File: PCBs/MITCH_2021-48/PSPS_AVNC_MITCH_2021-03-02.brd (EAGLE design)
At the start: 25.4 x 58.1 mm, 58 parts, among them J1 A-1JB, J2 TFM-107-01-XXX-D-DS, U0-C STM32F411CEUX, U1-S ICM-20948, U11-S SN74LV1T34, U12-S SN74LV1T34, U13-S SN74LV1T34, U14-S SN74LV1T34, U14-S1 SN74LV1T34, U14-S2 SN74LV1T34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

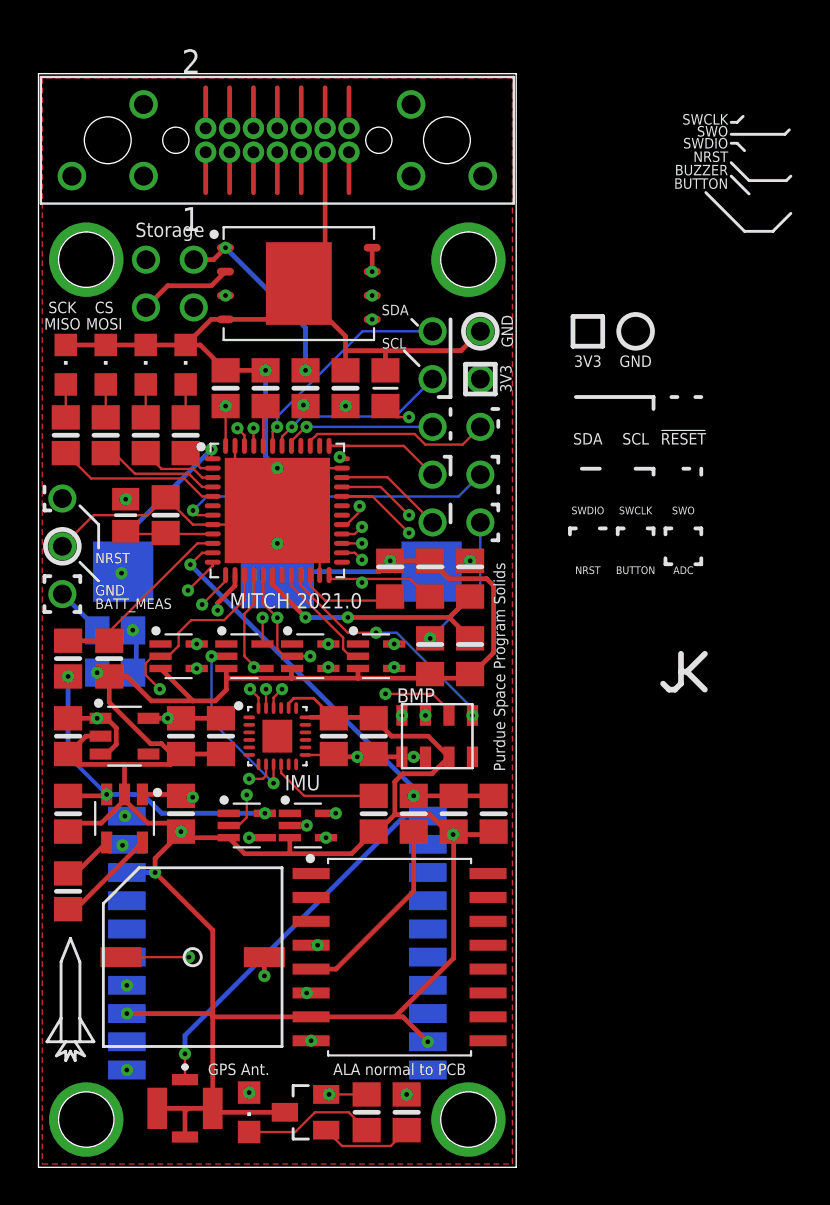
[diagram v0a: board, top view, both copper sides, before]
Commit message: Added separation notches
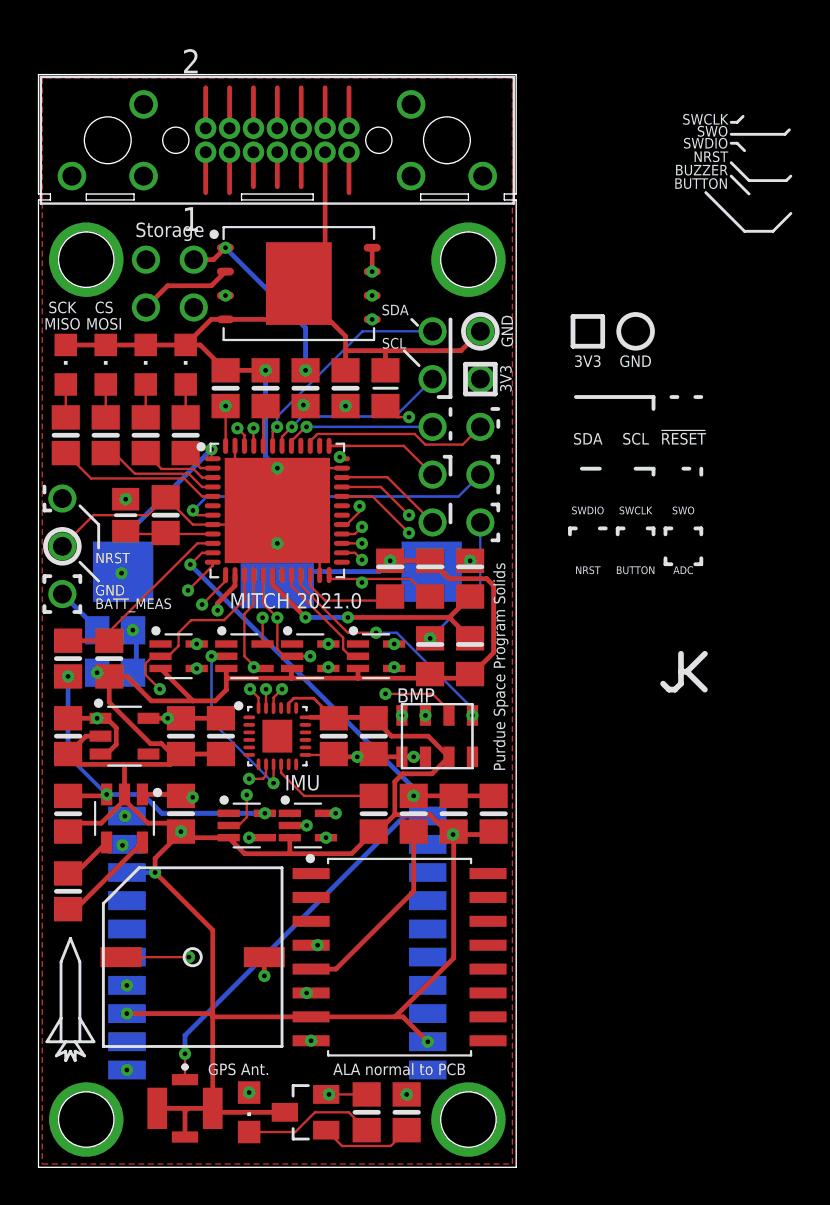
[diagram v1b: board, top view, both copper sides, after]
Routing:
- net BUTTON_IN: track 42.8 -> 44.6 mm
- net I2C_SCL: track 27.8 -> 29.3 mm
- net !RESET!: track 29.7 -> 31.2 mm
- net I2C_SDA: track 26.4 -> 27.8 mm
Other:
- outline, holes or cut-outs redrawn

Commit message: Improved Battery board interface nets
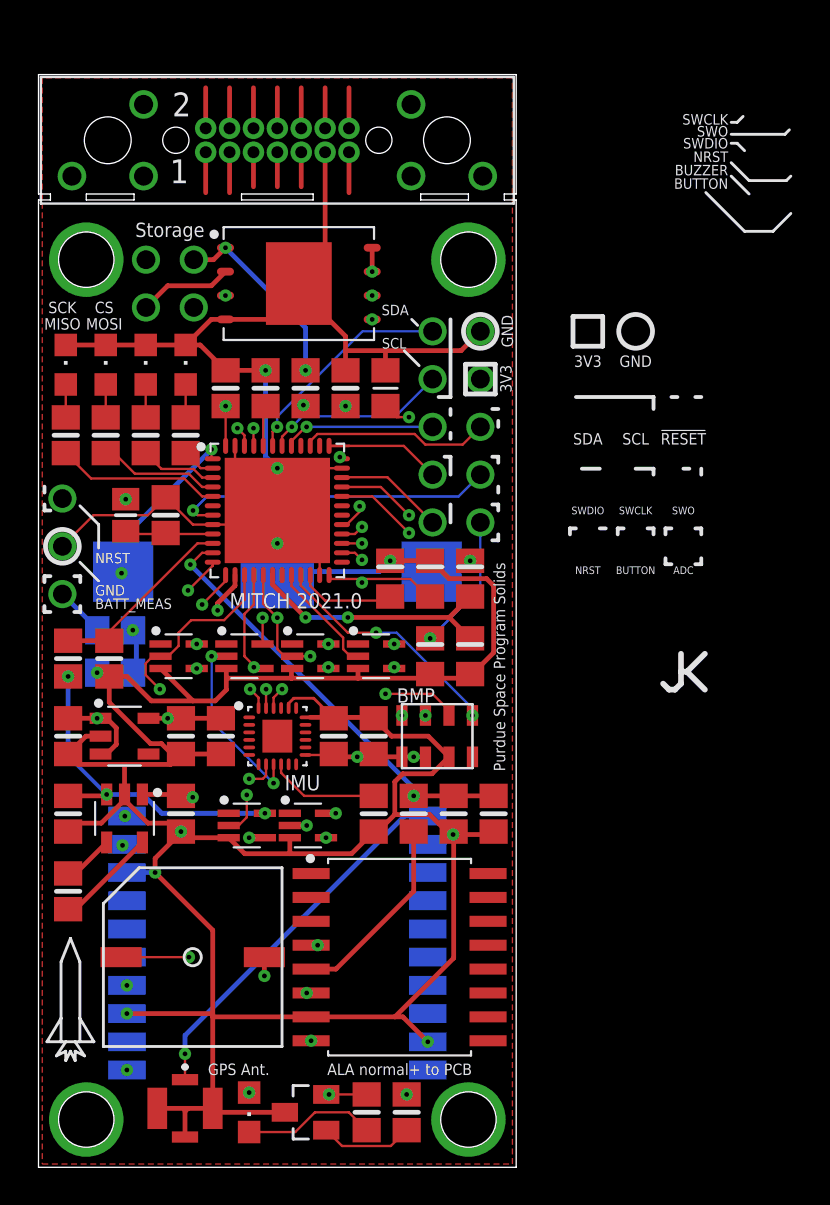
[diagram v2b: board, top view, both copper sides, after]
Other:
- board text added: "ALA normal+ to PCB"
- board text removed: "ALA normal to PCB"
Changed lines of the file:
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@@
 <layers>
 <layer number="1" name="Top" color="4" fill="1" visible="yes" active="yes"/>
-<layer number="2" name="Route2" color="16" fill="1" visible="yes" active="yes"/>
+<layer number="2" name="Route2" color="16" fill="1" visible="no" active="yes"/>
 <layer number="3" name="Route3" color="17" fill="1" visible="no" active="no"/>
 <layer number="4" name="Route4" color="18" fill="1" visible="no" active="no"/>
@@
 <layer number="13" name="Route13" color="21" fill="1" visible="no" active="no"/>
 <layer number="14" name="Route14" color="22" fill="1" visible="no" active="no"/>
-<layer number="15" name="Route15" color="23" fill="1" visible="yes" active="yes"/>
-<layer number="16" name="Bottom" color="1" fill="1" visible="yes" active="yes"/>
+<layer number="15" name="Route15" color="23" fill="1" visible="no" active="yes"/>
+<layer number="16" name="Bottom" color="1" fill="1" visible="no" active="yes"/>
 <layer number="17" name="Pads" color="2" fill="1" visible="yes" active="yes"/>
 <layer number="18" name="Vias" color="2" fill="1" visible="yes" active="yes"/>
@@
 <layer number="20" name="Dimension" color="24" fill="1" visible="yes" active="yes"/>
 <layer number="21" name="tPlace" color="7" fill="1" visible="yes" active="yes"/>
-<layer number="22" name="bPlace" color="7" fill="1" visible="yes" active="yes"/>
+<layer number="22" name="bPlace" color="7" fill="1" visible="no" active="yes"/>
 <layer number="23" name="tOrigins" color="15" fill="1" visible="yes" active="yes"/>
-<layer number="24" name="bOrigins" color="15" fill="1" visible="yes" active="yes"/>
+<layer number="24" name="bOrigins" color="15" fill="1" visible="no" active="yes"/>
 <layer number="25" name="tNames" color="7" fill="1" visible="yes" active="yes"/>
-<layer number="26" name="bNames" color="7" fill="1" visible="yes" active="yes"/>
+<layer number="26" name="bNames" color="7" fill="1" visible="no" active="yes"/>
 <layer number="27" name="tValues" color="7" fill="1" visible="no" active="yes"/>
 <layer number="28" name="bValues" color="7" fill="1" visible="no" active="yes"/>
@@
 <layer number="38" name="bTest" color="7" fill="1" visible="no" active="yes"/>
 <layer number="39" name="tKeepout" color="4" fill="11" visible="yes" active="yes"/>
-<layer number="40" name="bKeepout" color="1" fill="11" visible="yes" active="yes"/>
+<layer number="40" name="bKeepout" color="1" fill="11" visible="no" active="yes"/>
 <layer number="41" name="tRestrict" color="4" fill="10" visible="yes" active="yes"/>
-<layer number="42" name="bRestrict" color="1" fill="10" visible="yes" active="yes"/>
+<layer number="42" name="bRestrict" color="1" fill="10" visible="no" active="yes"/>
 <layer number="43" name="vRestrict" color="2" fill="10" visible="no" active="yes"/>
 <layer number="44" name="Drills" color="7" fill="1" visible="no" active="yes"/>
@@
 <layer number="50" name="dxf" color="7" fill="1" visible="no" active="no"/>
 <layer number="51" name="tDocu" color="7" fill="1" visible="yes" active="yes"/>
-<layer number="52" name="bDocu" color="7" fill="1" visible="yes" active="yes"/>
+<layer number="52" name="bDocu" color="7" fill="1" visible="no" active="yes"/>
 <layer number="53" name="tGND_GNDA" color="7" fill="9" visible="no" active="no"/>
 <layer number="54" name="bGND_GNDA" color="1" fill="9" visible="no" active="no"/>
@@
 <wire x1="-12.3825" y1="0.9525" x2="-12.3825" y2="1.27" width="0.2032" layer="22"/>
 <wire x1="-12.3825" y1="0" x2="-12.3825" y2="0.3175" width="0.2032" layer="22"/>
-<text x="6.5" y="-29.714" size="0.6096" layer="25" rot="R180" align="center">ALA normal to PCB</text>
+<text x="6.5" y="-29.714" size="0.6096" layer="25" rot="R180" align="center">ALA normal+ to PCB</text>
 <text x="1.3335" y="-14.474" size="0.8128" layer="25" rot="R180" align="center">IMU</text>
 <text x="7.366" y="-9.8365" size="0.762" layer="25" rot="R180" align="center">BMP</text>
